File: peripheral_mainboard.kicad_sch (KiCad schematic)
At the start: 33 parts, among them J5 AudioJack3, SW2 SW_SPST, SW3 SW_SPST, U5 TLV70033_SOT23-5, U6 PCM5102APW, U7 PAM8908

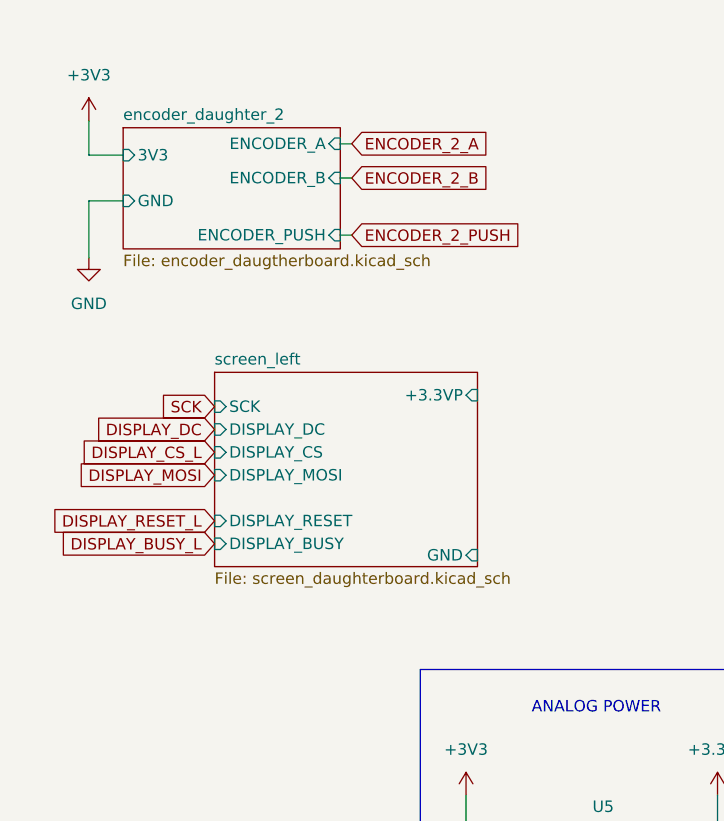
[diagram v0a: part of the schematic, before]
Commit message: fixed page numbers
and adjusted some label types
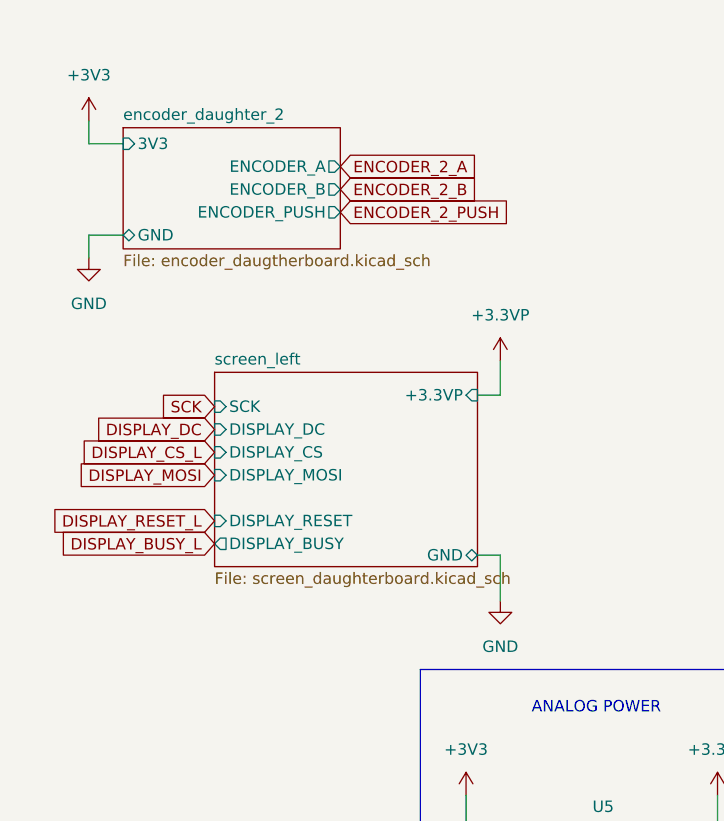
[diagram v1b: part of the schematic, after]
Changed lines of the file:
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@@
 	(wire
 		(pts
+			(xy 66.04 54.61) (xy 66.04 50.8)
+		)
+		(stroke
+			(width 0)
+			(type default)
+		)
+	)
+	(wire
+		(pts
 			(xy 124.46 95.25) (xy 123.19 95.25)
 		)
@@
 	(wire
 		(pts
-			(xy 20.32 27.94) (xy 24.13 27.94)
+			(xy 20.32 26.67) (xy 24.13 26.67)
 		)
 		(stroke
@@
 	(wire
 		(pts
-			(xy 20.32 24.13) (xy 20.32 27.94)
+			(xy 20.32 24.13) (xy 20.32 26.67)
 		)
 		(stroke
@@
 	(wire
 		(pts
-			(xy 48.26 36.83) (xy 49.53 36.83)
-		)
-		(stroke
-			(width 0)
-			(type default)
-		)
-	)
-	(wire
-		(pts
 			(xy 113.03 53.34) (xy 114.3 53.34)
 		)
@@
 	(wire
 		(pts
-			(xy 237.49 55.88) (xy 237.49 54.61)
+			(xy 20.32 36.83) (xy 24.13 36.83)
 		)
 		(stroke
@@
 	(wire
 		(pts
-			(xy 115.57 113.03) (xy 115.57 111.76)
+			(xy 237.49 55.88) (xy 237.49 54.61)
 		)
 		(stroke
@@
 	(wire
 		(pts
-			(xy 48.26 26.67) (xy 49.53 26.67)
+			(xy 115.57 113.03) (xy 115.57 111.76)
 		)
 		(stroke
@@
 	(wire
 		(pts
-			(xy 198.12 64.77) (xy 198.12 74.93)
+			(xy 63.5 54.61) (xy 66.04 54.61)
 		)
 		(stroke
@@
 	(wire
 		(pts
-			(xy 179.07 80.01) (xy 189.23 80.01)
+			(xy 198.12 64.77) (xy 198.12 74.93)
 		)
 		(stroke
@@
 	(wire
 		(pts
-			(xy 123.19 100.33) (xy 124.46 100.33)
+			(xy 179.07 80.01) (xy 189.23 80.01)
 		)
 		(stroke
@@
 	(wire
 		(pts
-			(xy 165.1 85.09) (xy 166.37 85.09)
+			(xy 123.19 100.33) (xy 124.46 100.33)
 		)
 		(stroke
@@
 	(wire
 		(pts
-			(xy 102.87 113.03) (xy 104.14 113.03)
+			(xy 165.1 85.09) (xy 166.37 85.09)
 		)
 		(stroke
@@
 	(wire
 		(pts
-			(xy 113.03 50.8) (xy 113.03 53.34)
+			(xy 102.87 113.03) (xy 104.14 113.03)
 		)
 		(stroke
@@
 	(wire
 		(pts
-			(xy 69.85 111.76) (xy 69.85 109.22)
+			(xy 113.03 50.8) (xy 113.03 53.34)
 		)
 		(stroke
@@
 	(wire
 		(pts
-			(xy 48.26 30.48) (xy 49.53 30.48)
+			(xy 69.85 111.76) (xy 69.85 109.22)
 		)
 		(stroke
@@
 	(wire
 		(pts
-			(xy 20.32 39.37) (xy 20.32 33.02)
+			(xy 113.03 58.42) (xy 113.03 55.88)
 		)
 		(stroke
@@
 	(wire
 		(pts
-			(xy 113.03 58.42) (xy 113.03 55.88)
+			(xy 113.03 55.88) (xy 113.03 53.34)
 		)
 		(stroke
@@
 	(wire
 		(pts
-			(xy 113.03 55.88) (xy 113.03 53.34)
+			(xy 113.03 48.26) (xy 114.3 48.26)
 		)
 		(stroke
@@
 	(wire
 		(pts
-			(xy 113.03 48.26) (xy 114.3 48.26)
+			(xy 66.04 72.39) (xy 66.04 77.47)
 		)
 		(stroke
@@
 	(wire
 		(pts
-			(xy 20.32 33.02) (xy 24.13 33.02)
+			(xy 20.32 36.83) (xy 20.32 39.37)
 		)
 		(stroke
@@
 	(wire
 		(pts
+			(xy 63.5 72.39) (xy 66.04 72.39)
+		)
+		(stroke
+			(width 0)
+			(type default)
+		)
+	)
+	(wire
+		(pts
 			(xy 165.1 77.47) (xy 171.45 77.47)
 		)
@@
 	(global_label "ENCODER_2_B"
 		(shape input)
-		(at 49.53 30.48 0)
+		(at 48.26 31.75 0)
 		(fields_autoplaced yes)
 		(effects
@@
 		)
 		(property "Intersheetrefs" "${INTERSHEET_REFS}"
-			(at 65.6989 30.48 0)
+			(at 64.4289 31.75 0)
 			(effects
 				(font
@@
 	(global_label "ENCODER_2_A"
 		(shape input)
-		(at 49.53 26.67 0)
+		(at 48.26 29.21 0)
 		(fields_autoplaced yes)
 		(effects
@@
 		)
 		(property "Intersheetrefs" "${INTERSHEET_REFS}"
-			(at 65.5175 26.67 0)
+			(at 64.2475 29.21 0)
 			(effects
 				(font
@@
 	(global_label "ENCODER_2_PUSH"
 		(shape input)
-		(at 49.53 36.83 0)
+		(at 48.26 34.29 0)
 		(fields_autoplaced yes)
 		(effects
@@
 		)
 		(property "Intersheetrefs" "${INTERSHEET_REFS}"
-			(at 69.5694 36.83 0)
+			(at 68.2994 34.29 0)
 			(effects
 				(font
@@
 	)
 	(symbol
+		(lib_id "power:GND")
+		(at 66.04 77.47 0)
+		(unit 1)
+		(exclude_from_sim no)
+		(in_bom yes)
+		(on_board yes)
+		(dnp no)
+		(fields_autoplaced yes)
+		(property "Reference" "#PWR0105"
+			(at 66.04 83.82 0)
+			(effects
+				(font
+					(size 1.27 1.27)
+				)
+				(hide yes)
+			)
+		)
+		(property "Value" "GND"
+			(at 66.04 82.55 0)
+			(effects
+				(font
+					(size 1.27 1.27)
+				)
+			)
+		)
+		(property "Footprint" ""
+			(at 66.04 77.47 0)
+			(effects
+				(font
+					(size 1.27 1.27)
+				)
+				(hide yes)
+			)
+		)
+		(property "Datasheet" ""
+			(at 66.04 77.47 0)
+			(effects
+				(font
+					(size 1.27 1.27)
+				)
+				(hide yes)
+			)
+		)
+		(property "Description" "Power symbol creates a global label with name \"GND\" , ground"
+			(at 66.04 77.47 0)
+			(effects
+				(font
+					(size 1.27 1.27)
+				)
+				(hide yes)
+			)
+		)
+		(pin "1"
+		)
+		(instances
+			(project "Tome"
+				(path "/2c6baa8c-bfd7-43e4-8688-255743ea3ca6/4b9dfd30-3edd-45e8-9d67-c2ad4f519ba5"
+					(reference "#PWR0105")
+					(unit 1)
+				)
+			)
+		)
+	)
+	(symbol
 		(lib_id "power:+3V3")
 		(at 62.23 99.06 0)
@@
 	)
 	(symbol
+		(lib_id "power:+3.3VP")
+		(at 66.04 50.8 0)
+		(unit 1)
+		(exclude_from_sim no)
+		(in_bom yes)
+		(on_board yes)
+		(dnp no)
+		(fields_autoplaced yes)
+		(property "Reference" "#PWR0104"
+			(at 69.85 52.07 0)
+			(effects
+				(font
+					(size 1.27 1.27)
+				)
+				(hide yes)
+			)
+		)
+		(property "Value" "+3.3VP"
+			(at 66.04 45.72 0)
+			(effects
+				(font
+					(size 1.27 1.27)
+				)
+			)
+		)
+		(property "Footprint" ""
+			(at 66.04 50.8 0)
+			(effects
+				(font
+					(size 1.27 1.27)
+				)
+				(hide yes)
+			)
+		)
+		(property "Datasheet" ""
+			(at 66.04 50.8 0)
+			(effects
+				(font
+					(size 1.27 1.27)
+				)
+				(hide yes)
+			)
+		)
+		(property "Description" "Power symbol creates a global label with name \"+3.3VP\""
+			(at 66.04 50.8 0)
+			(effects
+				(font
+					(size 1.27 1.27)
+				)
+				(hide yes)
+			)
+		)
+		(pin "1"
+		)
+		(instances
+			(project "Tome"
+				(path "/2c6baa8c-bfd7-43e4-8688-255743ea3ca6/4b9dfd30-3edd-45e8-9d67-c2ad4f519ba5"
+					(reference "#PWR0104")
+					(unit 1)
+				)
+			)
+		)
+	)
+	(symbol
 		(lib_id "Device:C_Small")
 		(at 90.17 111.76 0)
@@
 			)
 		)
-		(pin "DISPLAY_BUSY" input
-			(at 34.29 71.12 180)
-			(effects
-				(font
-					(size 1.27 1.27)
-				)
-				(justify left)
-			)
-		)
 		(pin "DISPLAY_RESET" input
 			(at 34.29 68.58 180)
@@
 			)
 		)
-		(pin "GND" input
+		(pin "DISPLAY_BUSY" output
+			(at 34.29 71.12 180)
+			(effects
+				(font
+					(size 1.27 1.27)
+				)
+				(justify left)
+			)
+		)
+		(pin "GND" bidirectional
 			(at 63.5 72.39 0)
 			(effects
@@
 			(project "Tome"
 				(path "/2c6baa8c-bfd7-43e4-8688-255743ea3ca6/4b9dfd30-3edd-45e8-9d67-c2ad4f519ba5"
-					(page "4")
+					(page "5")
 				)
 			)
@@
 			)
 		)
-		(pin "ENCODER_A" input
-			(at 48.26 26.67 0)
+		(pin "3V3" input
+			(at 24.13 26.67 180)
 			(effects
 				(font
 					(size 1.27 1.27)
 				)
-				(justify right)
+				(justify left)
 			)
 		)
-		(pin "ENCODER_B" input
-			(at 48.26 30.48 0)
+		(pin "ENCODER_PUSH" output
+			(at 48.26 34.29 0)
 			(effects
 				(font
@@
 			)
 		)
-		(pin "ENCODER_PUSH" input
-			(at 48.26 36.83 0)
+		(pin "ENCODER_A" output
+			(at 48.26 29.21 0)
 			(effects
 				(font
@@
 			)
 		)
-		(pin "3V3" input
-			(at 24.13 27.94 180)
+		(pin "ENCODER_B" output
+			(at 48.26 31.75 0)
 			(effects
 				(font
 					(size 1.27 1.27)
 				)
-				(justify left)
+				(justify right)
 			)
 		)
-		(pin "GND" input
-			(at 24.13 33.02 180)
+		(pin "GND" bidirectional
+			(at 24.13 36.83 180)
 			(effects
 				(font
@@
 			(project "Tome"
 				(path "/2c6baa8c-bfd7-43e4-8688-255743ea3ca6/4b9dfd30-3edd-45e8-9d67-c2ad4f519ba5"
-					(page "3")
+					(page "7")
 				)
 			)

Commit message: separating schematics based on board
finished splitting every component up into separate sheets in the schematic based on what physical board it's going on
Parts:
- added J9: Conn_01x17_Socket, symbol Connector:Conn_01x17_Socket
- added SW7: SW_SPST, symbol Switch:SW_SPST
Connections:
- net +3V3 is gone; now on net +3.3VP: C18.1, C38.1, C39.2, R22.1, U5.1 (IN), U6.20 (DVDD)
- net AUDIO_ENABLE is gone; now on net +3.3VP: U5.3 (EN)
- net +3.3VP: now also J9.1 (Pin_1)
- net AMP_ENABLE: now also J9.11 (Pin_11)
- net DISPLAY_BUSY_L: now also J9.10 (Pin_10)
- net DISPLAY_CS_L: now also J9.7 (Pin_7)
- net DISPLAY_DC: now also J9.6 (Pin_6)
- net DISPLAY_MOSI: now also J9.8 (Pin_8)
- net DISPLAY_RESET_L: now also J9.9 (Pin_9)
- net ENCODER_2_A: now also J9.4 (Pin_4)
- net ENCODER_2_B: now also J9.3 (Pin_3)
- net ENCODER_2_PUSH: now also J9.2 (Pin_2)
- net GND: now also J9.17 (Pin_17), SW7.2 (B)
- net I2S_BCK: now also J9.13 (Pin_13)
- net I2S_DATA: now also J9.12 (Pin_12)
- net I2S_LRCK: now also J9.15 (Pin_15)
- net SCK: now also J9.14 (Pin_14), J9.5 (Pin_5)
- new net: J9.16 (Pin_16), SW7.1 (A)
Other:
- sheet encoder_daughter_2 ports: added V_IN; removed 3V3
- sheet screen_left ports: added V_IN; removed +3.3VP
- note added: "ENCODER DAUGHTERBOARD"
- note added: "INTERCONNECT"
- note added: "SCREEN DAUGHTERBOARD"
- note added: "function switch"
- moved on the sheet: C18, C19, C20, C21, C22, C23, C24, C25, C26, C27, C28, C29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

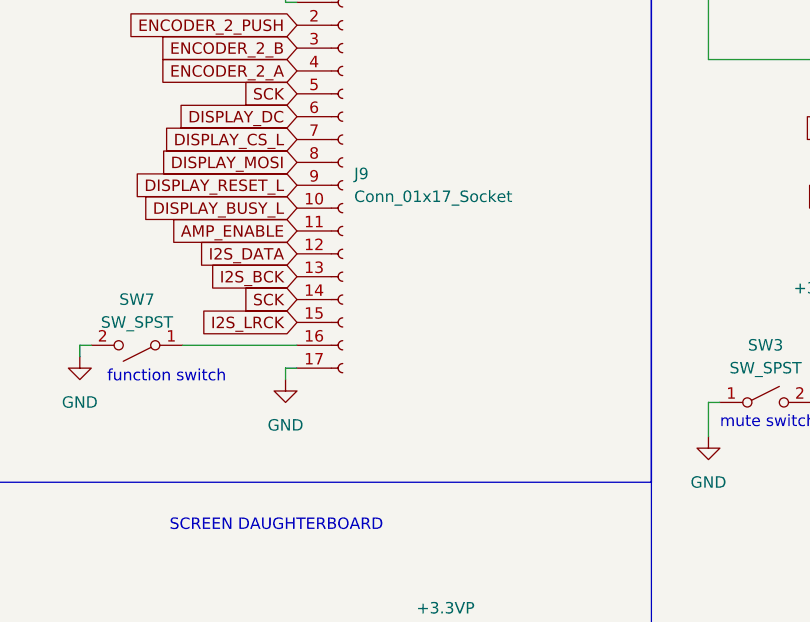
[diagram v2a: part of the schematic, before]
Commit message: assigning pcb footprints
assigned pcb footprints to most components:

- rotary encoder footprint will need slight modification to fit bourns PEC11L

- need to finalize components for reset button and the four switches before assigning those footprints
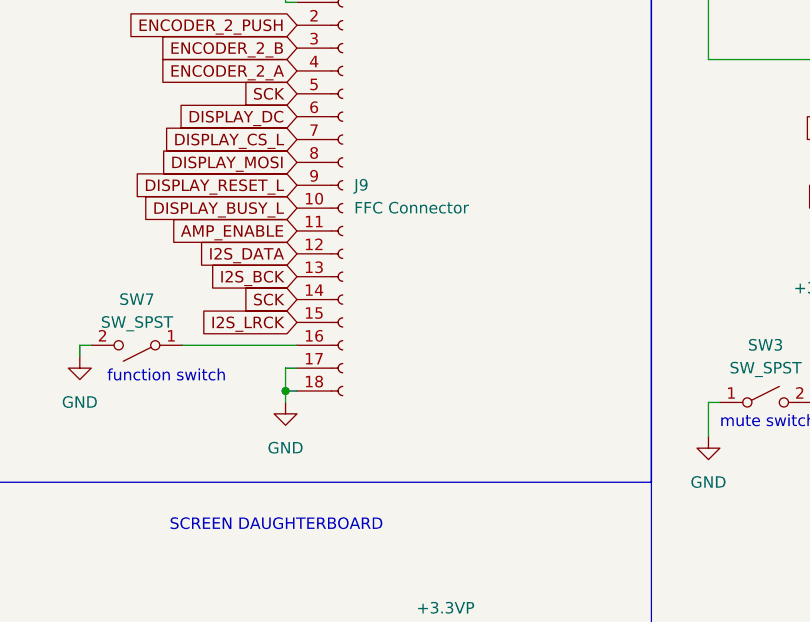
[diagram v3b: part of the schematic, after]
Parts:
- C18, C19, C20, C21, C22, C23, C24, C25, C26, C29, C30: footprint (none) -> Capacitor_SMD:C_0805_2012Metric
- C27, C28, C31: footprint (none) -> Capacitor_SMD:C_0402_1005Metric
- C32, C33, C36, C39: footprint (none) -> Capacitor_SMD:C_1206_3216Metric
- C34, C35, C37, C38: footprint (none) -> Capacitor_SMD:CP_Elec_4x4.5
- J5: footprint (none) -> Connector_Audio:Jack_3.5mm_CUI_SJ1-3523N_Horizontal
- J9: value Conn_01x17_Socket -> FFC Connector; footprint (none) -> Connector_FFC-FPC:JUSHUO_AFA07-S18FCA-00_1x18-1MP_P1.0mm_Horizontal; symbol Connector:Conn_01x17_Socket -> Connector:Conn_01x18_Socket
- R17, R18, R22: footprint (none) -> Resistor_SMD:R_1206_3216Metric
- R19, R20: footprint (none) -> Resistor_SMD:R_0603_1608Metric
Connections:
- net GND: now also J9.18 (Pin_18)
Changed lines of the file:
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@@
 	)
 	(junction
+		(at 57.15 124.46)
+		(diameter 0)
+		(color 0 0 0 0)
+	)
+	(junction
 		(at 193.04 72.39)
 		(diameter 0)
@@
 		)
 	)
+	(wire
+		(pts
+			(xy 57.15 124.46) (xy 57.15 121.92)
+		)
+		(stroke
+			(width 0)
+			(type default)
+		)
+	)
 	(polyline
 		(pts
@@
 	(wire
 		(pts
-			(xy 57.15 123.19) (xy 57.15 121.92)
+			(xy 57.15 125.73) (xy 57.15 124.46)
 		)
 		(stroke
@@
 	(wire
 		(pts
+			(xy 57.15 124.46) (xy 58.42 124.46)
+		)
+		(stroke
+			(width 0)
+			(type default)
+		)
+	)
+	(wire
+		(pts
 			(xy 184.15 82.55) (xy 201.93 82.55)
 		)
@@
 			)
 		)
-		(property "Footprint" ""
+		(property "Footprint" "Capacitor_SMD:CP_Elec_4x4.5"
 			(at 118.11 55.88 0)
 			(effects
@@
 			)
 		)
-		(property "Footprint" ""
+		(property "Footprint" "Capacitor_SMD:C_0805_2012Metric"
 			(at 247.65 101.6 0)
 			(effects
@@
 			)
 		)
-		(property "Footprint" ""
+		(property "Footprint" "Capacitor_SMD:CP_Elec_4x4.5"
 			(at 107.95 63.5 0)
 			(effects
@@
 			)
 		)
-		(property "Footprint" ""
+		(property "Footprint" "Resistor_SMD:R_1206_3216Metric"
 			(at 200.66 62.23 0)
 			(effects
@@
 			)
 		)
-		(property "Footprint" ""
+		(property "Footprint" "Capacitor_SMD:C_0805_2012Metric"
 			(at 238.76 71.12 0)
 			(effects
@@
 			)
 		)
-		(property "Footprint" ""
+		(property "Footprint" "Capacitor_SMD:C_0805_2012Metric"
 			(at 204.47 87.63 0)
 			(effects
@@
 			)
 		)
-		(property "Footprint" ""
+		(property "Footprint" "Capacitor_SMD:C_0805_2012Metric"
 			(at 204.47 92.71 0)
 			(effects
@@
 			)
 		)
-		(property "Footprint" ""
+		(property "Footprint" "Capacitor_SMD:C_0402_1005Metric"
 			(at 167.64 101.6 0)
 			(effects
@@
 			)
 		)
-		(property "Footprint" ""
+		(property "Footprint" "Capacitor_SMD:C_0402_1005Metric"
 			(at 218.44 54.61 0)
 			(effects
@@
 			)
 		)
-		(property "Footprint" ""
+		(property "Footprint" "Capacitor_SMD:CP_Elec_4x4.5"
 			(at 171.45 66.04 0)
 			(effects
@@
 			)
 		)
-		(property "Footprint" ""
+		(property "Footprint" "Capacitor_SMD:C_0805_2012Metric"
 			(at 190.5 101.6 0)
 			(effects
@@
 			)
 		)
-		(property "Footprint" ""
+		(property "Footprint" "Capacitor_SMD:C_0805_2012Metric"
 			(at 204.47 77.47 0)
 			(effects
@@
 			)
 		)
-		(property "Footprint" ""
+		(property "Footprint" "Connector_Audio:Jack_3.5mm_CUI_SJ1-3523N_Horizontal"
 			(at 262.89 86.36 0)
 			(effects
@@
 			)
 		)
-		(property "Footprint" ""
+		(property "Footprint" "Resistor_SMD:R_0603_1608Metric"
 			(at 175.26 90.17 0)
 			(effects
@@
 			)
 		)
-		(property "Footprint" ""
+		(property "Footprint" "Resistor_SMD:R_1206_3216Metric"
 			(at 193.04 62.23 0)
 			(effects
@@
 			)
 		)
-		(property "Footprint" ""
+		(property "Footprint" "Capacitor_SMD:C_0402_1005Metric"
 			(at 170.18 113.03 0)
 			(effects
@@
 			)
 		)
-		(property "Footprint" ""
+		(property "Footprint" "Capacitor_SMD:C_0805_2012Metric"
 			(at 204.47 82.55 0)
 			(effects
@@
 			)
 		)
-		(property "Footprint" ""
+		(property "Footprint" "Capacitor_SMD:C_0805_2012Metric"
 			(at 238.76 101.6 0)
 			(effects
@@
 			)
 		)
-		(property "Footprint" ""
+		(property "Footprint" "Resistor_SMD:R_1206_3216Metric"
 			(at 116.84 121.92 0)
 			(effects
@@
 	)
 	(symbol
-		(lib_id "Connector:Conn_01x17_Socket")
+		(lib_id "Connector:Conn_01x18_Socket")
 		(at 63.5 101.6 0)
 		(unit 1)
@@
 		(fields_autoplaced yes)
 		(property "Reference" "J9"
-			(at 64.77 100.3299 0)
+			(at 64.77 101.5999 0)
 			(effects
 				(font
@@
 			)
 		)
-		(property "Value" "Conn_01x17_Socket"
-			(at 64.77 102.8699 0)
+		(property "Value" "FFC Connector"
+			(at 64.77 104.1399 0)
 			(effects
 				(font
@@
 			)
 		)
-		(property "Footprint" ""
+		(property "Footprint" "Connector_FFC-FPC:JUSHUO_AFA07-S18FCA-00_1x18-1MP_P1.0mm_Horizontal"
 			(at 63.5 101.6 0)
 			(effects
@@
 			)
 		)
-		(property "Description" "Generic connector, single row, 01x17, script generated"
+		(property "Description" "Generic connector, single row, 01x18, script generated"
 			(at 63.5 101.6 0)
 			(effects
@@
 		(pin "17"
 		)
+		(pin "18"
+		)
 		(instances
 			(project ""
@@
 			)
 		)
-		(property "Footprint" ""
+		(property "Footprint" "Capacitor_SMD:C_0805_2012Metric"
 			(at 184.15 101.6 0)
 			(effects
@@
 			)
 		)
-		(property "Footprint" ""
+		(property "Footprint" "Capacitor_SMD:C_1206_3216Metric"
 			(at 107.95 68.58 0)
 			(effects
@@
 			)
 		)
-		(property "Footprint" ""
+		(property "Footprint" "Capacitor_SMD:C_1206_3216Metric"
 			(at 118.11 66.04 0)
 			(effects
@@
 			)
 		)
-		(property "Footprint" ""
+		(property "Footprint" "Capacitor_SMD:C_0805_2012Metric"
 			(at 39.37 39.37 0)
 			(effects
@@
 			)
 		)
-		(property "Footprint" ""
+		(property "Footprint" "Capacitor_SMD:CP_Elec_4x4.5"
 			(at 118.11 71.12 0)
 			(effects
@@
 			)
 		)
-		(property "Footprint" ""
+		(property "Footprint" "Capacitor_SMD:C_0805_2012Metric"
 			(at 67.31 39.37 0)
 			(effects
@@
 	(symbol
 		(lib_id "power:GND")
-		(at 57.15 123.19 0)
+		(at 57.15 125.73 0)
 		(unit 1)
 		(exclude_from_sim no)
@@
 		(fields_autoplaced yes)
 		(property "Reference" "#PWR0108"
-			(at 57.15 129.54 0)
+			(at 57.15 132.08 0)
 			(effects
 				(font
@@
 		)
 		(property "Value" "GND"
-			(at 57.15 128.27 0)
+			(at 57.15 130.81 0)
 			(effects
 				(font
@@
 		)
 		(property "Footprint" ""
-			(at 57.15 123.19 0)
+			(at 57.15 125.73 0)
 			(effects
 				(font
@@
 		)
 		(property "Datasheet" ""
-			(at 57.15 123.19 0)
+			(at 57.15 125.73 0)
 			(effects
 				(font
@@
 		)
 		(property "Description" "Power symbol creates a global label with name \"GND\" , ground"
-			(at 57.15 123.19 0)
+			(at 57.15 125.73 0)
 			(effects
 				(font
@@
 			)
 		)
-		(property "Footprint" ""
+		(property "Footprint" "Capacitor_SMD:C_1206_3216Metric"
 			(at 171.45 71.12 0)
 			(effects
@@
 			)
 		)
-		(property "Footprint" ""
+		(property "Footprint" "Capacitor_SMD:C_1206_3216Metric"
 			(at 118.11 60.96 0)
 			(effects
@@
 			)
 		)
-		(property "Footprint" ""
+		(property "Footprint" "Resistor_SMD:R_0603_1608Metric"
 			(at 175.26 85.09 0)
 			(effects
